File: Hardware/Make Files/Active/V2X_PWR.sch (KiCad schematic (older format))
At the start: 55 parts, among them P10 Board Mount 2, P11 Ficudial2, P12 Board Mount 3, P13 Ficudial3, P14 5V0_OUT, P15 Board Mount 4, P16 Ficudial4, P17 CUR_SEN, P19 CUR_SEN, P6 Board Mount 1, P7 Ficudial1, P9 USB_u, Q11 IRF9335, Q13 BSS84, Q14 IRF9335, Q15 2N7000, SW2 SW_PUSH, U11 XRP6124, U12 SLG59M, U15 SLG59M, U16 SLG59M, U17 XRP6124, U18 SLG59M

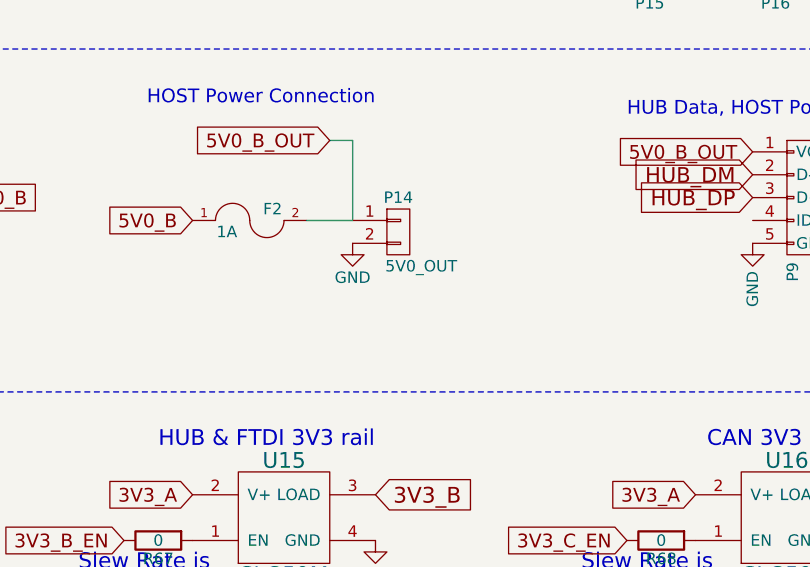
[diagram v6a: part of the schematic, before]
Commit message: Added USB-A to design
discovered the Rpi cannot be back fed over USB, had to add a power Port
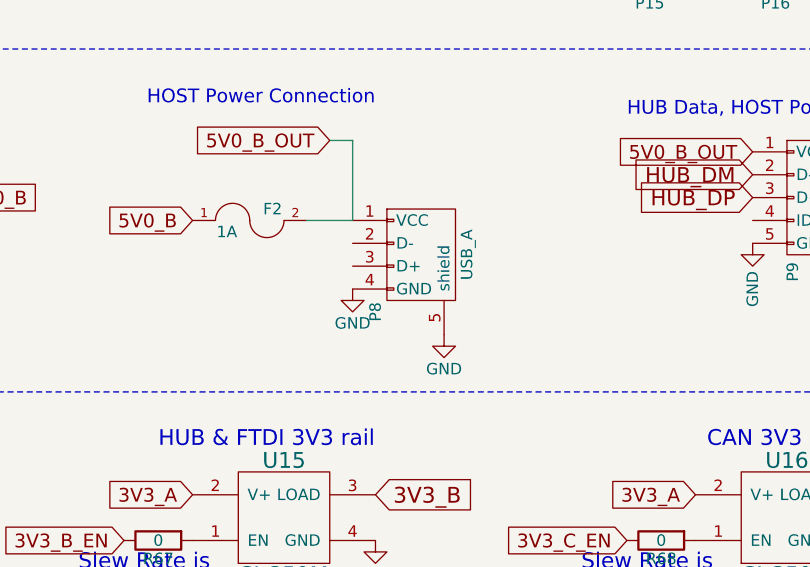
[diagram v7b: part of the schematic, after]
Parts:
- removed P14: 5V0_OUT, Connect:PINHEAD1-2, symbol CONN_01X02
- added P8: USB_A, Connect:USB_A, symbol USB_A
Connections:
- net 5V0_B_OUT: now also P8.1 (VCC)
- net GND: now also P8.4 (GND), P8.5 (shield)
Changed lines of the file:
@@
 $Descr USLetter 11000 8500
 encoding utf-8
-Sheet 4 7
+Sheet 4 8
 Title "V2X - Open source RVI over SMS daughter card"
 Date "2015-07-17"
@@
 L GND #PWR055
 U 1 1 55C7D0D4
-P 7700 2700
-F 0 "#PWR055" H 7700 2450 50  0001 C CNN
-F 1 "GND" H 7700 2550 50  0000 C CNN
-F 2 "" H 7700 2700 60  0000 C CNN
-F 3 "" H 7700 2700 60  0000 C CNN
-	1    7700 2700
+P 7700 2900
+F 0 "#PWR055" H 7700 2650 50  0001 C CNN
+F 1 "GND" H 7700 2750 50  0000 C CNN
+F 2 "" H 7700 2900 60  0000 C CNN
+F 3 "" H 7700 2900 60  0000 C CNN
+	1    7700 2900
 	1    0    0    -1
 $EndComp
@@
 	0    -1   1    0
 $EndComp
-$Comp
-L CONN_01X02 P14
-U 1 1 56108001
-P 7900 2650
-F 0 "P14" H 7900 2800 50  0000 C CNN
-F 1 "5V0_OUT" H 8000 2500 50  0000 C CNN
-F 2 "Connect:PINHEAD1-2" H 7900 2650 60  0001 C CNN
-F 3 "http://www.mouser.com/ds/2/276/0022285023_PCB_HEADERS-159058.pdf" H 7900 2650 60  0001 C CNN
-F 4 "538-22-28-5023" H 7900 2650 60  0001 C CNN "Mouse PN"
-	1    7900 2650
-	1    0    0    -1
-$EndComp
 Wire Wire Line
 	5900 2500 5950 2500
+$Comp
+L USB_A P8
+U 1 1 561FEF14
+P 8000 2800
+F 0 "P8" H 8200 2600 50  0000 C CNN
+F 1 "USB_A" H 7950 3000 50  0000 C CNN
+F 2 "Connect:USB_A" V 7950 2700 60  0001 C CNN
+F 3 "" V 7950 2700 60  0000 C CNN
+	1    8000 2800
+	0    1    1    0
+$EndComp
+$Comp
+L GND #PWR075
+U 1 1 561FF7A1
+P 8100 3100
+F 0 "#PWR075" H 8100 2850 50  0001 C CNN
+F 1 "GND" H 8100 2950 50  0000 C CNN
+F 2 "" H 8100 3100 60  0000 C CNN
+F 3 "" H 8100 3100 60  0000 C CNN
+	1    8100 3100
+	1    0    0    -1
+$EndComp
 $EndSCHEMATC

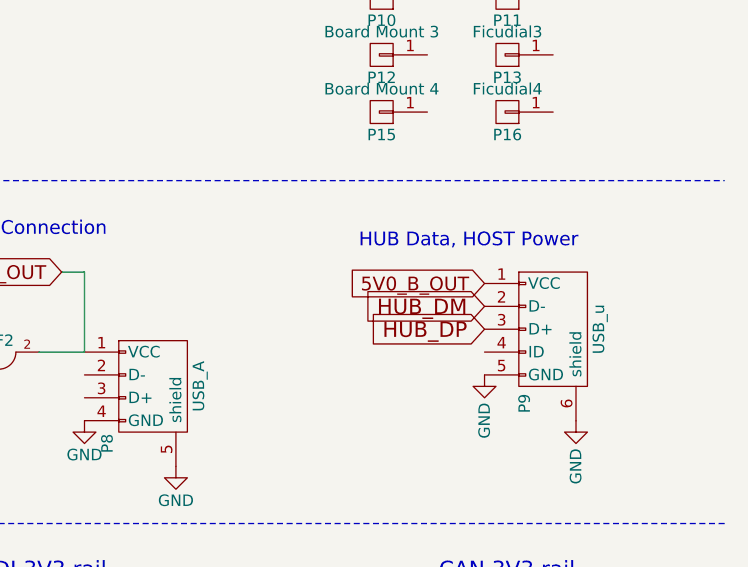
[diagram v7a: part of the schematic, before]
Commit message: No Rpi Backpower fix
added a USB-A to the board to power the HOST. fixed LED labeling.
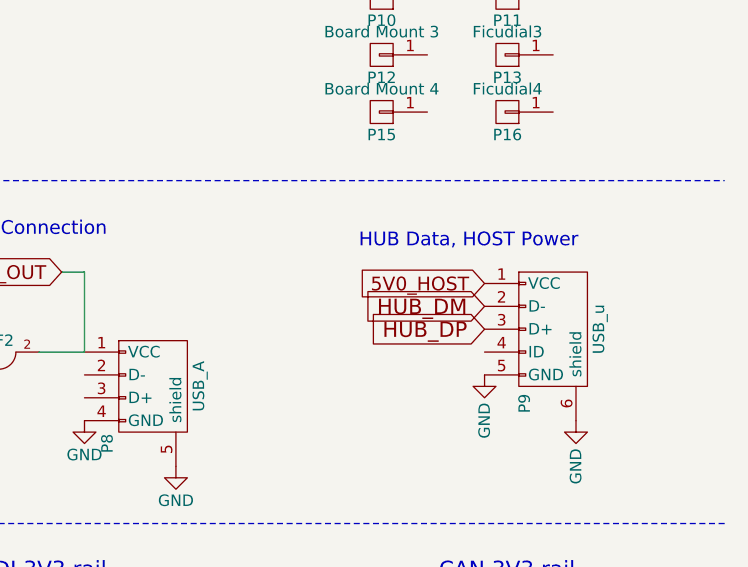
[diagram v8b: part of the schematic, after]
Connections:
- net 5V0_B_OUT: no longer P9.1 (VCC)
- new net 5V0_HOST: P9.1 (VCC)
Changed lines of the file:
@@
 EESchema Schematic File Version 2
 LIBS:V2X-rescue
-LIBS:sim5320_KICAD_PART
-LIBS:CUSTOM_KICAD_PART
 LIBS:74xgxx
 LIBS:74xx
@@
 LIBS:xilinx
 LIBS:Zilog
+LIBS:CUSTOM_KICAD_PART
 LIBS:V2X-cache
 EELAYER 25 0
@@
 Connection ~ 2900 1050
 $Comp
-L GND #PWR052
+L GND #PWR051
 U 1 1 55AAAD3C
 P 1700 1400
-F 0 "#PWR052" H 1700 1150 50  0001 C CNN
+F 0 "#PWR051" H 1700 1150 50  0001 C CNN
 F 1 "GND" H 1700 1250 50  0000 C CNN
 F 2 "" H 1700 1400 60  0000 C CNN
@@
 $EndComp
 $Comp
-L GND #PWR053
+L GND #PWR052
 U 1 1 55AAAECD
 P 2400 1500
-F 0 "#PWR053" H 2400 1250 50  0001 C CNN
+F 0 "#PWR052" H 2400 1250 50  0001 C CNN
 F 1 "GND" H 2400 1350 50  0000 C CNN
 F 2 "" H 2400 1500 60  0000 C CNN
@@
 $EndComp
 $Comp
-L GND #PWR054
+L GND #PWR053
 U 1 1 55AAAF11
 P 2900 1450
-F 0 "#PWR054" H 2900 1200 50  0001 C CNN
+F 0 "#PWR053" H 2900 1200 50  0001 C CNN
 F 1 "GND" H 2900 1300 50  0000 C CNN
 F 2 "" H 2900 1450 60  0000 C CNN
@@
 3.3V @ 1A DC-DC Power Supply
 $Comp
-L GND #PWR055
+L GND #PWR054
 U 1 1 55C7D0D4
 P 7700 2900
-F 0 "#PWR055" H 7700 2650 50  0001 C CNN
+F 0 "#PWR054" H 7700 2650 50  0001 C CNN
 F 1 "GND" H 7700 2750 50  0000 C CNN
 F 2 "" H 7700 2900 60  0000 C CNN
@@
 $EndComp
 $Comp
-L GND #PWR056
+L GND #PWR055
 U 1 1 55FBBA0A
 P 1350 2400
-F 0 "#PWR056" H 1350 2150 50  0001 C CNN
+F 0 "#PWR055" H 1350 2150 50  0001 C CNN
 F 1 "GND" V 1350 2200 50  0000 C CNN
 F 2 "" H 1350 2400 60  0000 C CNN
@@
 $EndComp
 $Comp
-L GND #PWR057
+L GND #PWR056
 U 1 1 55FBBA10
 P 3450 3100
-F 0 "#PWR057" H 3450 2850 50  0001 C CNN
+F 0 "#PWR056" H 3450 2850 50  0001 C CNN
 F 1 "GND" H 3450 2950 50  0000 C CNN
 F 2 "" H 3450 3100 60  0000 C CNN
@@
 Connection ~ 2800 2300
 $Comp
-L GND #PWR058
+L GND #PWR057
 U 1 1 55FBBA33
 P 2800 2600
-F 0 "#PWR058" H 2800 2350 50  0001 C CNN
+F 0 "#PWR057" H 2800 2350 50  0001 C CNN
 F 1 "GND" H 2950 2550 50  0000 C CNN
 F 2 "" H 2800 2600 60  0000 C CNN
@@
 $EndComp
 $Comp
-L GND #PWR059
+L GND #PWR058
 U 1 1 55FBBA3F
 P 2250 2800
-F 0 "#PWR059" H 2250 2550 50  0001 C CNN
+F 0 "#PWR058" H 2250 2550 50  0001 C CNN
 F 1 "GND" V 2250 2600 50  0000 C CNN
 F 2 "" H 2250 2800 60  0000 C CNN
@@
 Connection ~ 1300 2800
 $Comp
-L GND #PWR060
+L GND #PWR059
 U 1 1 55FBBA68
 P 950 2800
-F 0 "#PWR060" H 950 2550 50  0001 C CNN
+F 0 "#PWR059" H 950 2550 50  0001 C CNN
 F 1 "GND" V 950 2600 50  0000 C CNN
 F 2 "" H 950 2800 60  0000 C CNN
@@
 5V0_A
 $Comp
-L GND #PWR061
+L GND #PWR060
 U 1 1 55FBD5DC
 P 3450 4050
-F 0 "#PWR061" H 3450 3800 50  0001 C CNN
+F 0 "#PWR060" H 3450 3800 50  0001 C CNN
 F 1 "GND" V 3450 3850 50  0000 C CNN
 F 2 "" H 3450 4050 60  0000 C CNN
@@
 $EndComp
 $Comp
-L GND #PWR062
+L GND #PWR061
 U 1 1 55FBD5E2
 P 5550 4750
-F 0 "#PWR062" H 5550 4500 50  0001 C CNN
+F 0 "#PWR061" H 5550 4500 50  0001 C CNN
 F 1 "GND" H 5550 4600 50  0000 C CNN
 F 2 "" H 5550 4750 60  0000 C CNN
@@
 $EndComp
 $Comp
-L GND #PWR063
+L GND #PWR062
 U 1 1 55FBD605
 P 4900 4250
-F 0 "#PWR063" H 4900 4000 50  0001 C CNN
+F 0 "#PWR062" H 4900 4000 50  0001 C CNN
 F 1 "GND" H 5050 4200 50  0000 C CNN
 F 2 "" H 4900 4250 60  0000 C CNN
@@
 $EndComp
 $Comp
-L GND #PWR064
+L GND #PWR063
 U 1 1 55FBD611
 P 4350 4450
-F 0 "#PWR064" H 4350 4200 50  0001 C CNN
+F 0 "#PWR063" H 4350 4200 50  0001 C CNN
 F 1 "GND" V 4350 4250 50  0000 C CNN
 F 2 "" H 4350 4450 60  0000 C CNN
@@
 	3400 4150 3450 4150
 $Comp
-L GND #PWR065
+L GND #PWR064
 U 1 1 55FBD63A
 P 3450 5050
-F 0 "#PWR065" H 3450 4800 50  0001 C CNN
+F 0 "#PWR064" H 3450 4800 50  0001 C CNN
 F 1 "GND" V 3450 4850 50  0000 C CNN
 F 2 "" H 3450 5050 60  0000 C CNN
@@
 5V0_B_EN
 $Comp
-L GND #PWR066
+L GND #PWR065
 U 1 1 55FC949A
 P 5900 2700
-F 0 "#PWR066" H 5900 2450 50  0001 C CNN
+F 0 "#PWR065" H 5900 2450 50  0001 C CNN
 F 1 "GND" H 5900 2550 50  0000 C CNN
 F 2 "" H 5900 2700 60  0000 C CNN
@@
 $EndComp
 $Comp
-L GND #PWR067
+L GND #PWR066
 U 1 1 55FCD01A
 P 1350 4750
-F 0 "#PWR067" H 1350 4500 50  0001 C CNN
+F 0 "#PWR066" H 1350 4500 50  0001 C CNN
 F 1 "GND" V 1450 4700 50  0000 C CNN
 F 2 "" H 1350 4750 60  0000 C CNN
@@
 $EndComp
 $Comp
-L GND #PWR068
+L GND #PWR067
 U 1 1 55FCEBFC
 P 7800 4000
-F 0 "#PWR068" H 7800 3750 50  0001 C CNN
+F 0 "#PWR067" H 7800 3750 50  0001 C CNN
 F 1 "GND" H 7800 3850 50  0000 C CNN
 F 2 "" H 7800 4000 60  0000 C CNN
@@
 $EndComp
 $Comp
-L GND #PWR069
+L GND #PWR068
 U 1 1 5600FC76
 P 2000 4300
-F 0 "#PWR069" H 2000 4050 50  0001 C CNN
+F 0 "#PWR068" H 2000 4050 50  0001 C CNN
 F 1 "GND" V 2100 4250 50  0000 C CNN
 F 2 "" H 2000 4300 60  0000 C CNN
@@
 	1700 4550 1700 4600
 $Comp
-L GND #PWR070
+L GND #PWR069
 U 1 1 56011CFE
 P 1700 4900
-F 0 "#PWR070" H 1700 4650 50  0001 C CNN
+F 0 "#PWR069" H 1700 4650 50  0001 C CNN
 F 1 "GND" H 1700 4750 50  0000 C CNN
 F 2 "" H 1700 4900 60  0000 C CNN
@@
 3V3_C
 $Comp
-L GND #PWR071
+L GND #PWR070
 U 1 1 5604ED5E
 P 10000 4000
-F 0 "#PWR071" H 10000 3750 50  0001 C CNN
+F 0 "#PWR070" H 10000 3750 50  0001 C CNN
 F 1 "GND" H 10000 3850 50  0000 C CNN
 F 2 "" H 10000 4000 60  0000 C CNN
@@
 HUB_DP
 $Comp
-L GND #PWR072
+L GND #PWR071
 U 1 1 5604F800
 P 9850 2900
-F 0 "#PWR072" H 9850 2650 50  0001 C CNN
+F 0 "#PWR071" H 9850 2650 50  0001 C CNN
 F 1 "GND" V 9850 2700 50  0000 C CNN
 F 2 "" H 9850 2900 60  0000 C CNN
@@
 $EndComp
 $Comp
-L GND #PWR073
+L GND #PWR072
 U 1 1 5604F806
 P 9450 2700
-F 0 "#PWR073" H 9450 2450 50  0001 C CNN
+F 0 "#PWR072" H 9450 2450 50  0001 C CNN
 F 1 "GND" V 9450 2500 50  0000 C CNN
 F 2 "" H 9450 2700 60  0000 C CNN
@@
 Text Notes 8900 2150 0    60   ~ 0
 HUB Data, HOST Power
-Text GLabel 9450 2300 0    60   Input ~ 0
-5V0_B_OUT
 Wire Notes Line
 	500  1850 10500 1850
@@
 3V3_D
 $Comp
-L GND #PWR074
+L GND #PWR073
 U 1 1 56057D75
 P 10000 5000
-F 0 "#PWR074" H 10000 4750 50  0001 C CNN
+F 0 "#PWR073" H 10000 4750 50  0001 C CNN
 F 1 "GND" H 10000 4850 50  0000 C CNN
 F 2 "" H 10000 5000 60  0000 C CNN
@@
 $EndComp
 $Comp
-L GND #PWR075
+L GND #PWR074
 U 1 1 561FF7A1
 P 8100 3100
-F 0 "#PWR075" H 8100 2850 50  0001 C CNN
+F 0 "#PWR074" H 8100 2850 50  0001 C CNN
 F 1 "GND" H 8100 2950 50  0000 C CNN
 F 2 "" H 8100 3100 60  0000 C CNN
@@
 	1    0    0    -1
 $EndComp
+Text GLabel 9450 2300 0    60   Input ~ 0
+5V0_HOST
 $EndSCHEMATC
